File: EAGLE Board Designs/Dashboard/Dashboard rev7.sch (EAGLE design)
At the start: 108 parts, among them J1 CONNECTOR-4_μF_S_RA_, J2 CONNECTOR-8_μF_S_RA_, J3 CONNECTOR-4_μF_S_RA_, J4 CONNECTOR-6_μF_S_RA_, J5 CONNECTOR-12_MF_T_V_, J6 CONNECTOR-6_μF_S_RA_, J7 CONNECTOR-4_538-505110-0492_, J8 USB4110, U1 NEOPIXEL_IN-PI55QATPRPGPBPW-40, U10 NEOPIXEL_IN-PI55QATPRPGPBPW-40, U11 NEOPIXEL_IN-PI55QATPRPGPBPW-40, U12 NEOPIXEL_IN-PI55QATPRPGPBPW-40, U13 NEOPIXEL_IN-PI55QATPRPGPBPW-40, U14 NEOPIXEL_IN-PI55QATPRPGPBPW-40, U15 NEOPIXEL_IN-PI55QATPRPGPBPW-40, U16 STM32-LQFP64, U17 VOLTAGE_REGULATOR_SOT-223_3.3V, U2 NEOPIXEL_IN-PI55QATPRPGPBPW-40, U27 TCAN1051HQV-Q1, U3 MCP23S08, U4 NEOPIXEL_IN-PI55QATPRPGPBPW-40, U5 RE46C100, U6 NEOPIXEL_IN-PI55QATPRPGPBPW-40, U7 NEOPIXEL_IN-PI55QATPRPGPBPW-40, U8 NEOPIXEL_IN-PI55QATPRPGPBPW-40, U9 NEOPIXEL_IN-PI55QATPRPGPBPW-40, X1 24_MHZ_XTAL_OSCILLATOR

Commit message: More Routing
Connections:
- removed net N$2: C14.1
- net BOTS_READ: now also U16.PB6; no longer U16.PB5
- net BRB_READ: now also U16.PB5; no longer U16.PB7
- net INERTIA_READ: now also U16.PB7; no longer U16.PB6
- net MCU_NRST: now also C14.1
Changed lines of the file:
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@@
 <pinref part="R7" gate="G$1" pin="1"/>
 <wire x1="198.12" y1="185.42" x2="198.12" y2="182.88" width="0.1524" layer="91"/>
-<wire x1="198.12" y1="182.88" x2="185.42" y2="182.88" width="0.1524" layer="91"/>
+<wire x1="198.12" y1="182.88" x2="187.96" y2="182.88" width="0.1524" layer="91"/>
 <label x="185.42" y="182.88" size="1.27" layer="95" font="vector" rot="R180" xref="yes"/>
+<wire x1="187.96" y1="182.88" x2="185.42" y2="182.88" width="0.1524" layer="91"/>
 <wire x1="198.12" y1="182.88" x2="198.12" y2="180.34" width="0.1524" layer="91"/>
 <junction x="198.12" y="182.88"/>
 <pinref part="S1" gate="G$1" pin="P"/>
+<pinref part="C14" gate="G$1" pin="1"/>
+<wire x1="187.96" y1="180.34" x2="187.96" y2="182.88" width="0.1524" layer="91"/>
+<junction x="187.96" y="182.88"/>
 </segment>
 </net>
@@
 </segment>
 </net>
-<net name="N$2" class="0">
-<segment>
-<pinref part="C14" gate="G$1" pin="1"/>
-<wire x1="187.96" y1="180.34" x2="187.96" y2="182.88" width="0.1524" layer="91"/>
-</segment>
-</net>
 <net name="BTN_MODE_READ" class="0">
 <segment>
@@
 <wire x1="119.38" y1="175.26" x2="119.38" y2="177.8" width="0.1524" layer="91"/>
 <label x="119.38" y="177.8" size="1.27" layer="95" rot="R90" xref="yes"/>
-</segment>
-</net>
-<net name="BOTS_READ" class="0">
-<segment>
-<pinref part="U16" gate="G$1" pin="PB5"/>
-<wire x1="109.22" y1="175.26" x2="109.22" y2="177.8" width="0.1524" layer="91"/>
-<label x="109.22" y="177.8" size="1.27" layer="95" rot="R90" xref="yes"/>
-</segment>
-</net>
-<net name="INERTIA_READ" class="0">
-<segment>
-<pinref part="U16" gate="G$1" pin="PB6"/>
-<wire x1="106.68" y1="175.26" x2="106.68" y2="177.8" width="0.1524" layer="91"/>
-<label x="106.68" y="177.8" size="1.27" layer="95" rot="R90" xref="yes"/>
-</segment>
-</net>
-<net name="BRB_READ" class="0">
-<segment>
-<pinref part="U16" gate="G$1" pin="PB7"/>
-<wire x1="104.14" y1="175.26" x2="104.14" y2="177.8" width="0.1524" layer="91"/>
-<label x="104.14" y="177.8" size="1.27" layer="95" font="vector" rot="R90" xref="yes"/>
 </segment>
 </net>
@@
 </segment>
 </net>
+<net name="BOTS_READ" class="0">
+<segment>
+<wire x1="106.68" y1="175.26" x2="106.68" y2="177.8" width="0.1524" layer="91"/>
+<label x="106.68" y="177.8" size="1.27" layer="95" rot="R90" xref="yes"/>
+<pinref part="U16" gate="G$1" pin="PB6"/>
+</segment>
+</net>
+<net name="INERTIA_READ" class="0">
+<segment>
+<wire x1="104.14" y1="175.26" x2="104.14" y2="177.8" width="0.1524" layer="91"/>
+<label x="104.14" y="177.8" size="1.27" layer="95" rot="R90" xref="yes"/>
+<pinref part="U16" gate="G$1" pin="PB7"/>
+</segment>
+</net>
+<net name="BRB_READ" class="0">
+<segment>
+<wire x1="109.22" y1="175.26" x2="109.22" y2="177.8" width="0.1524" layer="91"/>
+<label x="109.22" y="177.8" size="1.27" layer="95" font="vector" rot="R90" xref="yes"/>
+<pinref part="U16" gate="G$1" pin="PB5"/>
+</segment>
+</net>

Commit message: Almost Finished routing, added new parts and added second display connectors
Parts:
- added C26, C27: CAPACITOR_0603_10V_0.1UF, HyTechDevices:CAPACITOR_0603_10V_0.1UF
- added J10: CONNECTOR-10__, HyTechDevices:CONNECTOR-10__
- added J9: CONNECTOR-4_538-505110-0492_, HyTechDevices:CONNECTOR-4_538-505110-0492_
- added TP7, TP8: TEST_POINT, HyTechDevices:TEST_POINT
- J5: value CONNECTOR-12_MF_T_V_ -> CONNECTOR-10__; device HyTechDevices:CONNECTOR-12_MF_T_V_ -> HyTechDevices:CONNECTOR-10__
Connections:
- removed net N$29: J7.3, J7.4
- removed net N$34: C18.1, C19.1, J5.5, J5.6, J5.7
- net +5V: now also C18.1, C19.1, C26.1, C27.1, J10.5, J10.6, J10.7, J5.5, J5.6, J5.7, J9.1, J9.2
- net GND: now also C26.2, C27.2, J10.10, J10.9, J7.3, J7.4, J9.3, J9.4; no longer J5.11, J5.12
- net MCU_SPI3_MOSI: now also J10.2, TP8.1
- net MCU_SPI3_SCK: now also J10.1, TP7.1
- net SHARP_CS: now also J10.3
- net SHARP_EXTMODE: now also J10.8
- net SHARP_VCOMM: now also J10.4
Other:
- note added: "Backlight 1"
- note added: "Backlight 2"
- note removed: "Backlight"

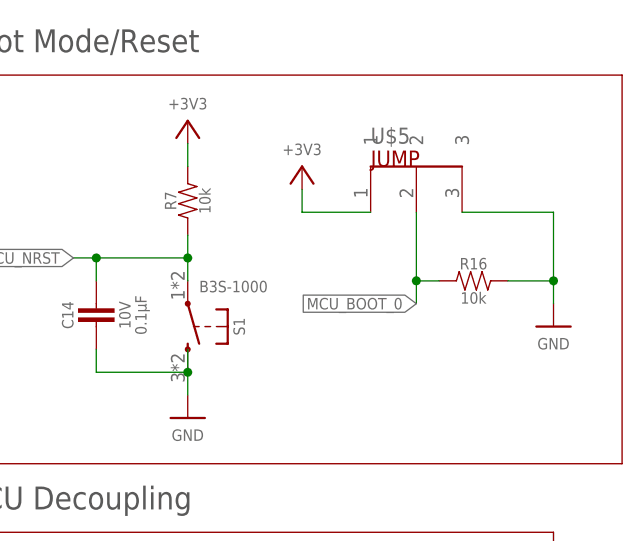
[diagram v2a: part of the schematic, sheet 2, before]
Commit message: Finished routing dash rev 7
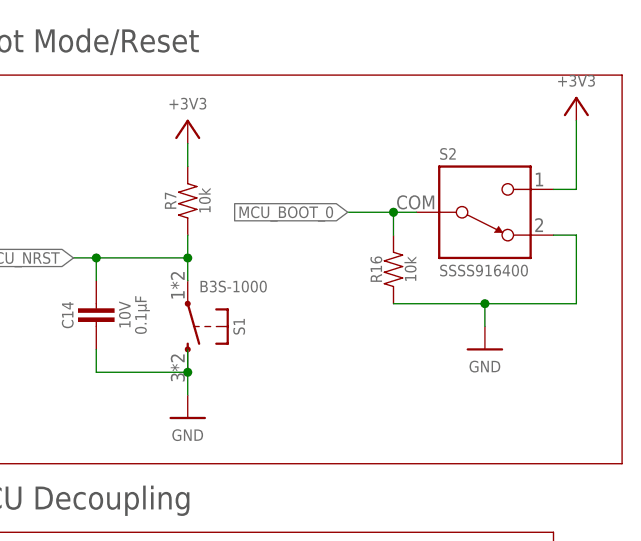
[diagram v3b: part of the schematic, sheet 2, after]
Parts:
- removed U$5: JUMPER_3PIN, HyTechDevices:JUMPER_3PIN
- removed U11: NEOPIXEL_IN-PI55QATPRPGPBPW-40, HyTechDevices:NEOPIXEL_IN-PI55QATPRPGPBPW-40
- added R19, R20: RESISTOR_0603_30, HyTechDevices:RESISTOR_0603_30
- added S2: SWITCH_SPDT_SSSS916400, HyTechDevices:SWITCH_SPDT_SSSS916400
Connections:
- removed net N$9: U11.DOUT, U12.DIN
- new net N$16: J7.3, J7.4, R20.2
- new net N$17: J9.3, J9.4, R19.2
- net +3V3: now also S2.1; no longer U$5.1
- net +5V: no longer U11.VDD
- net GND: now also R16.1, R19.1, R20.1, S2.2; no longer J7.3, J7.4, J9.3, J9.4, R16.2, U$5.3, U11.GND
- net MCU_BOOT_0: now also R16.2, S2.COM; no longer R16.1, U$5.2
- net N$1: now also U12.DIN; no longer U11.DIN
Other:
- moved on the sheet: R16

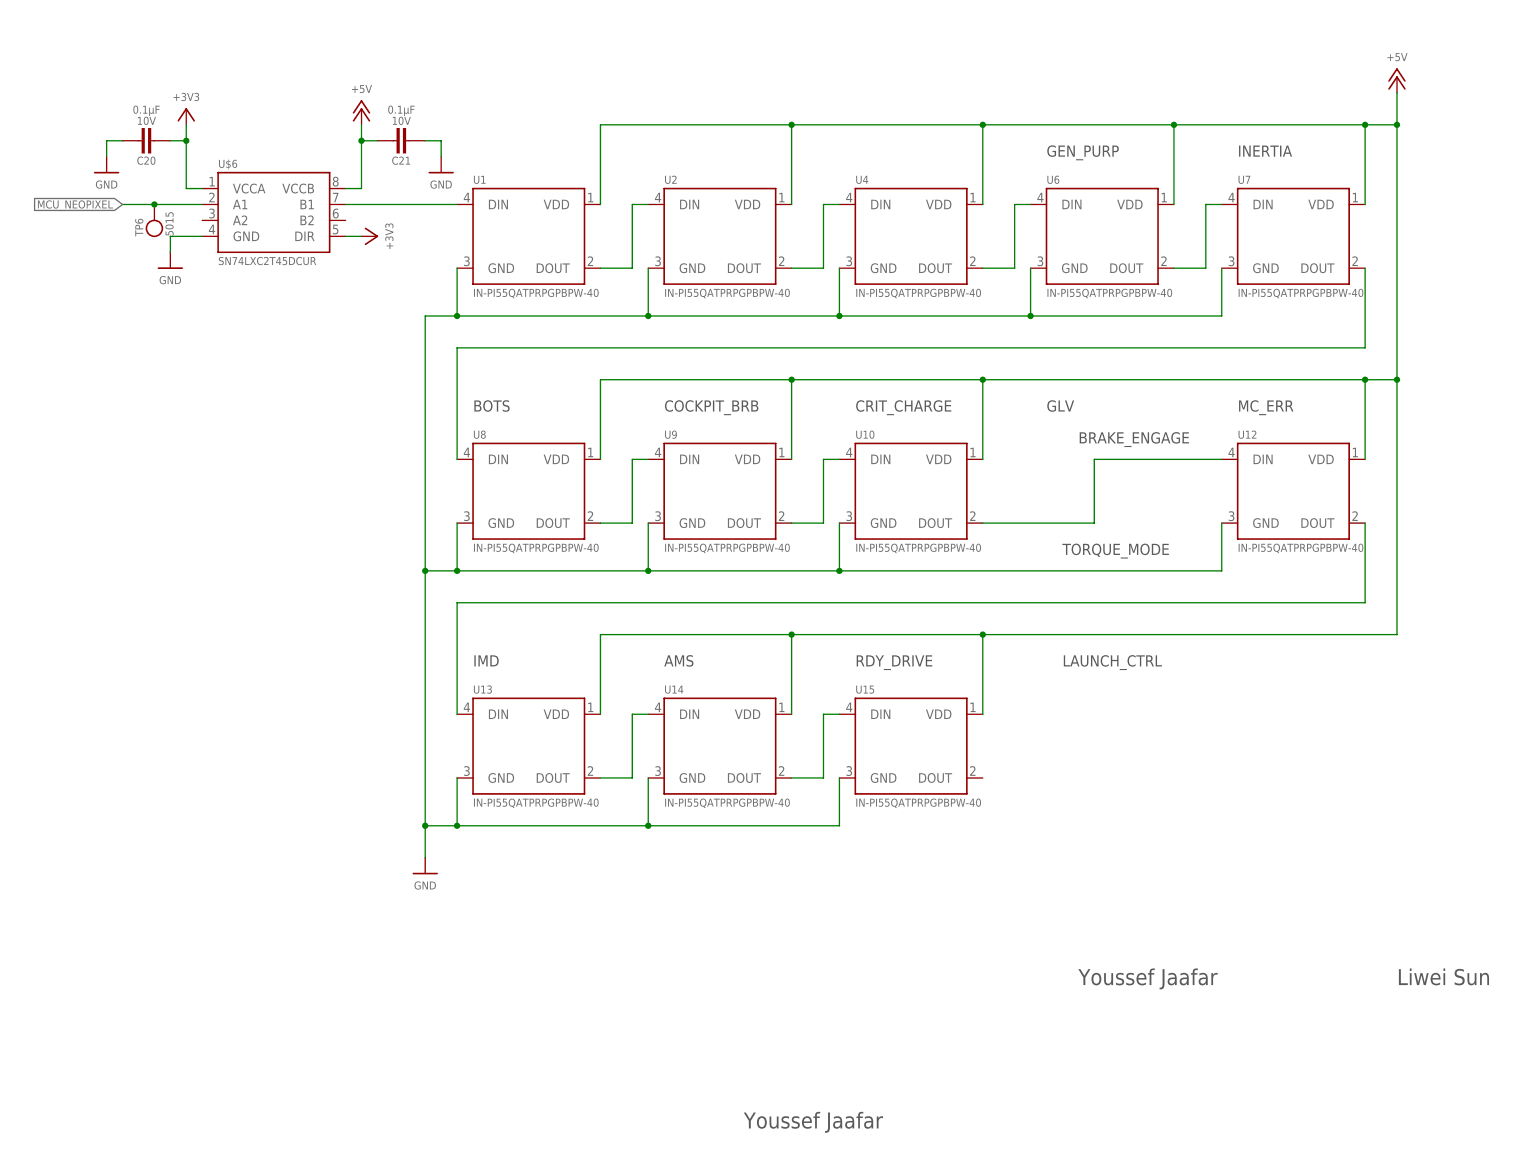
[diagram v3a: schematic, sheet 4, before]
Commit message: Fixes to power planes and routing
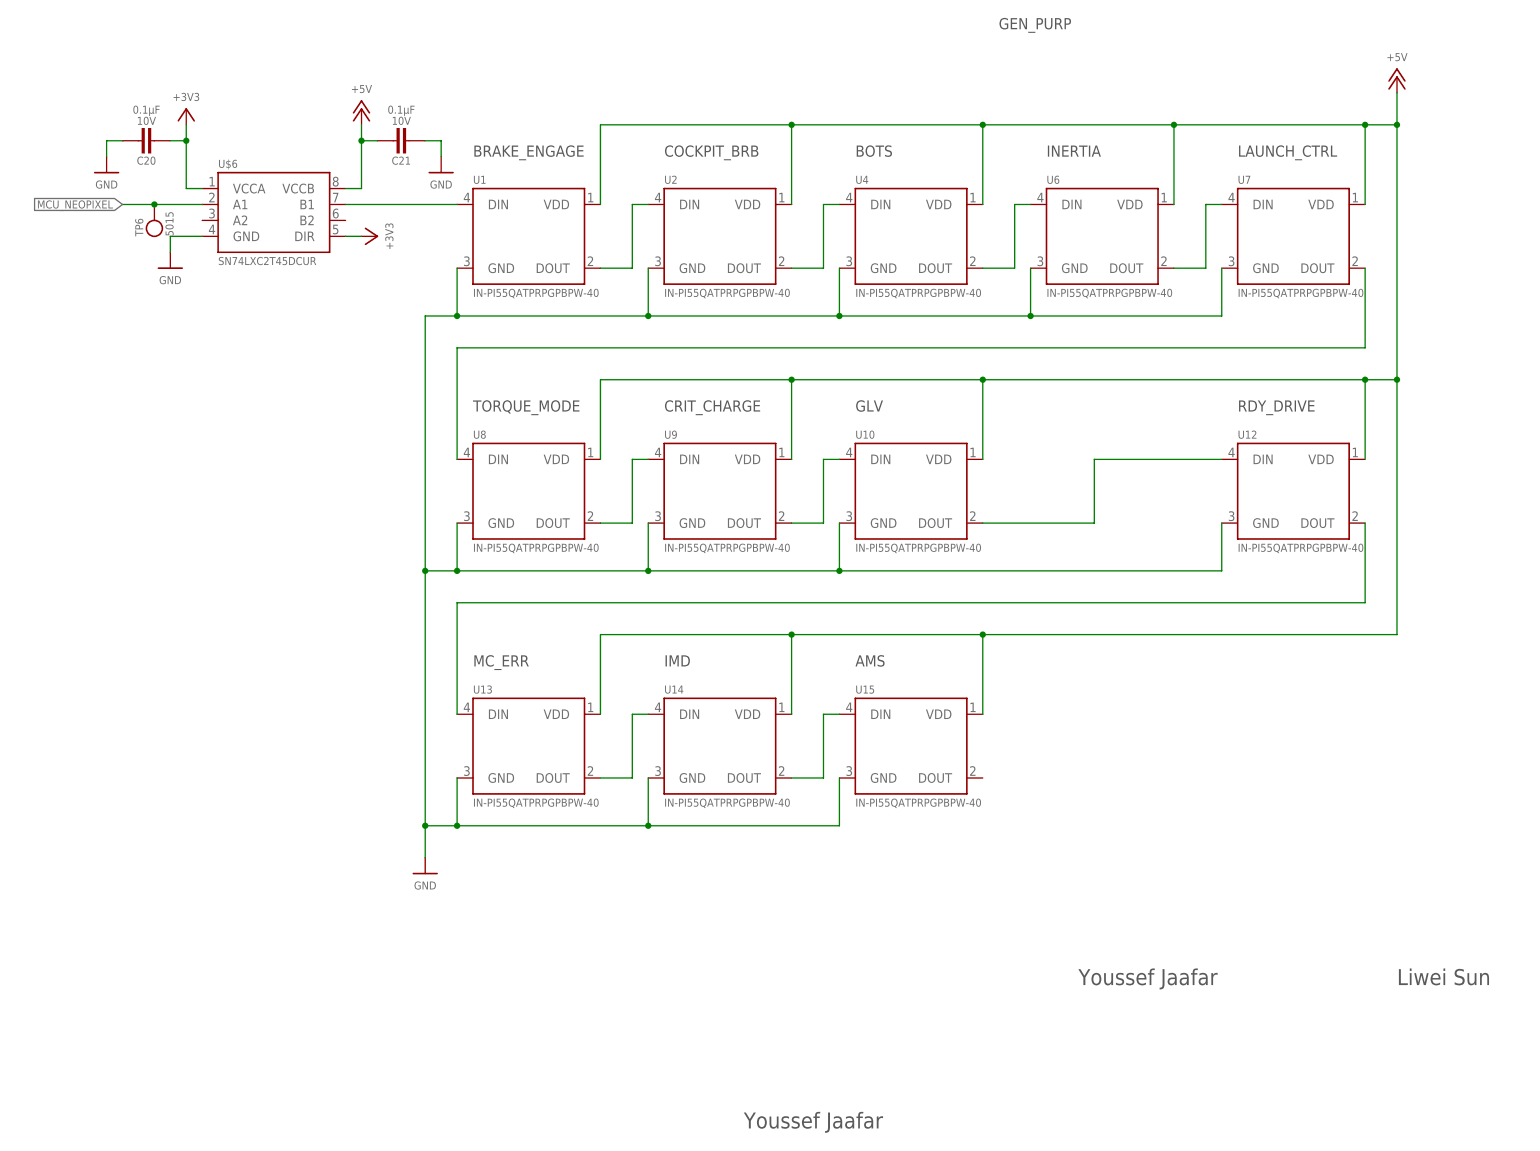
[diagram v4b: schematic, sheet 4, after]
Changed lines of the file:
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@@
 <description>Neopixels</description>
 <plain>
-<text x="180.34" y="177.8" size="1.778" layer="97">GEN_PURP</text>
-<text x="210.82" y="177.8" size="1.778" layer="97">INERTIA</text>
-<text x="88.9" y="137.16" size="1.778" layer="97">BOTS</text>
-<text x="119.38" y="137.16" size="1.778" layer="97">COCKPIT_BRB</text>
-<text x="119.38" y="96.52" size="1.778" layer="97">AMS</text>
-<text x="88.9" y="96.52" size="1.778" layer="97">IMD</text>
-<text x="210.82" y="137.16" size="1.778" layer="97">MC_ERR</text>
-<text x="149.86" y="137.16" size="1.778" layer="97">CRIT_CHARGE</text>
-<text x="182.88" y="114.3" size="1.778" layer="97">TORQUE_MODE</text>
-<text x="149.86" y="96.52" size="1.778" layer="97">RDY_DRIVE</text>
-<text x="180.34" y="137.16" size="1.778" layer="97">GLV</text>
-<text x="185.42" y="132.08" size="1.778" layer="97">BRAKE_ENGAGE</text>
-<text x="182.88" y="96.52" size="1.778" layer="97">LAUNCH_CTRL</text>
+<text x="172.72" y="198.12" size="1.778" layer="97">GEN_PURP</text>
+<text x="180.34" y="177.8" size="1.778" layer="97">INERTIA</text>
+<text x="149.86" y="177.8" size="1.778" layer="97">BOTS</text>
+<text x="119.38" y="177.8" size="1.778" layer="97">COCKPIT_BRB</text>
+<text x="149.86" y="96.52" size="1.778" layer="97">AMS</text>
+<text x="119.38" y="96.52" size="1.778" layer="97">IMD</text>
+<text x="88.9" y="96.52" size="1.778" layer="97">MC_ERR</text>
+<text x="119.38" y="137.16" size="1.778" layer="97">CRIT_CHARGE</text>
+<text x="88.9" y="137.16" size="1.778" layer="97">TORQUE_MODE</text>
+<text x="210.82" y="137.16" size="1.778" layer="97">RDY_DRIVE</text>
+<text x="149.86" y="137.16" size="1.778" layer="97">GLV</text>
+<text x="88.9" y="177.8" size="1.778" layer="97">BRAKE_ENGAGE</text>
+<text x="210.82" y="177.8" size="1.778" layer="97">LAUNCH_CTRL</text>
 <text x="236.22" y="45.72" size="2.54" layer="97">Liwei Sun</text>
 <text x="185.42" y="45.72" size="2.54" layer="97">Youssef Jaafar</text>
